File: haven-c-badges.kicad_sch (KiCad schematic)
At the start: 0 parts

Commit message: schematic done I think
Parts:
- added C1: 220nF, symbol Device:C
- added D1: LED, symbol Device:LED
- added L1: 25X48MM_NFC_ANTENNA, nfc_antenna:25X48MM_NFC_ANTENNA, symbol Device:L
- added R1: 47*, symbol Device:R
- added U1: NT3H2111W0FHKH, easyeda2kicad:XQFN-8_L1.6-W1.6-P0.50-BL_NT3H2111W0FHKH, symbol easyeda2kicad:NT3H2111W0FHKH
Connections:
- new net: C1.1, D1.1 (K), U1.2 (VSS)
- new net: D1.2 (A), R1.1
- new net: C1.2, R1.2, U1.6 (VCC), U1.7 (VOUT)
- new net: L1.2, U1.1 (LA)
- new net: L1.1, U1.8 (LB)
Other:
- note added: "NFC Stuff"
- note added: "This is from a guide I hope it isn't wrong"

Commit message: did some of that easyeda2kicad conversion and well.. yeah
- had some issues with courtyards and footprints not showing up
- set up env var paths I think
- i might just use part of notaroomba's library
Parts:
- C1: footprint (none) -> EasyEDA2Kicad:C0603
- D1: footprint (none) -> EasyEDA2Kicad:LED0805-R-RD
- L1: footprint nfc_antenna:25X48MM_NFC_ANTENNA -> EasyEDA2Kicad:25X48MM_NFC_ANTENNA manualimport
- R1: footprint (none) -> EasyEDA2Kicad:R0603
- U1: footprint easyeda2kicad:XQFN-8_L1.6-W1.6-P0.50-BL_NT3H2111W0FHKH -> EasyEDA2Kicad:XQFN-8_L1.6-W1.6-P0.50-BL_NT3H2111W0FHKH
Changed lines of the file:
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@@
 			)
 		)
-		(property "Footprint" ""
+		(property "Footprint" "EasyEDA2Kicad:LED0805-R-RD"
 			(at 107.95 123.19 0)
 			(hide yes)
@@
 			)
 		)
-		(property "Footprint" ""
+		(property "Footprint" "EasyEDA2Kicad:R0603"
 			(at 123.19 124.968 90)
 			(hide yes)
@@
 			)
 		)
-		(property "Footprint" ""
+		(property "Footprint" "EasyEDA2Kicad:C0603"
 			(at 119.38 108.2548 0)
 			(hide yes)
@@
 			)
 		)
-		(property "Footprint" "easyeda2kicad:XQFN-8_L1.6-W1.6-P0.50-BL_NT3H2111W0FHKH"
+		(property "Footprint" "EasyEDA2Kicad:XQFN-8_L1.6-W1.6-P0.50-BL_NT3H2111W0FHKH"
 			(at 115.57 100.33 0)
 			(hide yes)
@@
 			)
 		)
-		(property "Footprint" "nfc_antenna:25X48MM_NFC_ANTENNA"
+		(property "Footprint" "EasyEDA2Kicad:25X48MM_NFC_ANTENNA manualimport"
 			(at 115.57 66.04 0)
 			(hide yes)

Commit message: he was whipping up straight poison in a kettle
- WHY CANT I GET THESE TWO PADS TO CONNECT IDK ABOUT THE POLARITY pls help
- i switched all the footprints and symbols around like 3 times
- the antennas are wired up correctly now I think 💔(manual net assigning at the antenna pads)
a. polarity is not in antennas
b. but the nets not connected by default is rlly bugging me
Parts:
- removed U1: NT3H2111W0FHKH, EasyEDA2Kicad:XQFN-8_L1.6-W1.6-P0.50-BL_NT3H2111W0FHKH, symbol easyeda2kicad:NT3H2111W0FHKH
- added U1: NT3H2111W0FHKH, NFC Components:XQFN-8_L1.6-W1.6-P0.50-BL_NT3H2111W0FHKH, symbol NFC_components:NT3H2111W0FHKH
- L1: footprint EasyEDA2Kicad:25X48MM_NFC_ANTENNA manualimport -> NFC Components:25X48MM_NFC_ANTENNA
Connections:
- net at C1.1, D1.1 (K): now also U1.2 (VSS)
- net at C1.2, R1.2: now also U1.6 (VCC), U1.7 (VOUT)
- net at L1.2: now also U1.1 (LA)
- net at L1.1: now also U1.8 (LB)
- no-connect marks 0 -> 3
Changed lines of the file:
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@@
 		(color 0 0 0 0)
 	)
+	(no_connect
+		(at 105.41 90.17)
+	)
+	(no_connect
+		(at 105.41 92.71)
+	)
+	(no_connect
+		(at 125.73 92.71)
+	)
 	(wire
 		(pts
@@
 	(wire
 		(pts
-			(xy 129.54 66.04) (xy 119.38 66.04)
+			(xy 128.27 66.04) (xy 119.38 66.04)
 		)
 		(stroke
@@
 	(wire
 		(pts
-			(xy 101.6 85.09) (xy 105.41 85.09)
-		)
-		(stroke
-			(width 0)
-			(type default)
-		)
-	)
-	(wire
-		(pts
-			(xy 111.76 66.04) (xy 101.6 66.04)
-		)
-		(stroke
-			(width 0)
-			(type default)
-		)
-	)
-	(wire
-		(pts
-			(xy 125.73 85.09) (xy 129.54 85.09)
+			(xy 125.73 85.09) (xy 128.27 85.09)
+		)
+		(stroke
+			(width 0)
+			(type default)
+		)
+	)
+	(wire
+		(pts
+			(xy 111.76 66.04) (xy 102.87 66.04)
 		)
 		(stroke
@@
 	(wire
 		(pts
+			(xy 125.73 87.63) (xy 128.27 87.63)
+		)
+		(stroke
+			(width 0)
+			(type default)
+		)
+	)
+	(wire
+		(pts
 			(xy 100.33 87.63) (xy 100.33 123.19)
 		)
@@
 	(wire
 		(pts
-			(xy 129.54 85.09) (xy 129.54 66.04)
-		)
-		(stroke
-			(width 0)
-			(type default)
-		)
-	)
-	(wire
-		(pts
-			(xy 101.6 66.04) (xy 101.6 85.09)
-		)
-		(stroke
-			(width 0)
-			(type default)
-		)
-	)
-	(wire
-		(pts
-			(xy 127 87.63) (xy 125.73 87.63)
+			(xy 128.27 85.09) (xy 128.27 66.04)
+		)
+		(stroke
+			(width 0)
+			(type default)
+		)
+	)
+	(wire
+		(pts
+			(xy 102.87 66.04) (xy 102.87 85.09)
 		)
 		(stroke
@@
 	(wire
 		(pts
+			(xy 102.87 85.09) (xy 105.41 85.09)
+		)
+		(stroke
+			(width 0)
+			(type default)
+		)
+	)
+	(wire
+		(pts
 			(xy 100.33 87.63) (xy 102.87 87.63)
 		)
@@
 		(pts
 			(xy 111.76 123.19) (xy 119.38 123.19)
-		)
-		(stroke
-			(width 0)
-			(type default)
-		)
-	)
-	(wire
-		(pts
-			(xy 127 87.63) (xy 128.27 87.63)
 		)
 		(stroke
@@
 	)
 	(symbol
+		(lib_id "NFC_components:NT3H2111W0FHKH")
+		(at 115.57 88.9 0)
+		(unit 1)
+		(body_style 1)
+		(exclude_from_sim no)
+		(in_bom yes)
+		(on_board yes)
+		(in_pos_files yes)
+		(dnp no)
+		(fields_autoplaced yes)
+		(property "Reference" "U1"
+			(at 115.57 76.2 0)
+			(show_name no)
+			(do_not_autoplace no)
+			(effects
+				(font
+					(size 1.27 1.27)
+				)
+			)
+		)
+		(property "Value" "NT3H2111W0FHKH"
+			(at 115.57 78.74 0)
+			(show_name no)
+			(do_not_autoplace no)
+			(effects
+				(font
+					(size 1.27 1.27)
+				)
+			)
+		)
+		(property "Footprint" "NFC Components:XQFN-8_L1.6-W1.6-P0.50-BL_NT3H2111W0FHKH"
+			(at 115.57 100.33 0)
+			(hide yes)
+			(show_name no)
+			(do_not_autoplace no)
+			(effects
+				(font
+					(size 1.27 1.27)
+				)
+			)
+		)
+		(property "Datasheet" ""
+			(at 115.57 88.9 0)
+			(hide yes)
+			(show_name no)
+			(do_not_autoplace no)
+			(effects
+				(font
+					(size 1.27 1.27)
+				)
+			)
+		)
+		(property "Description" ""
+			(at 115.57 88.9 0)
+			(hide yes)
+			(show_name no)
+			(do_not_autoplace no)
+			(effects
+				(font
+					(size 1.27 1.27)
+				)
+			)
+		)
+		(property "LCSC Part" "C710403"
+			(at 115.57 102.87 0)
+			(hide yes)
+			(show_name no)
+			(do_not_autoplace no)
+			(effects
+				(font
+					(size 1.27 1.27)
+				)
+			)
+		)
+		(pin "2"
+		)
+		(pin "6"
+		)
+		(pin "3"
+		)
+		(pin "5"
+		)
+		(pin "8"
+		)
+		(pin "7"
+		)
+		(pin "1"
+		)
+		(pin "4"
+		)
+		(instances
+			(project "haven-c-badges"
+				(path "/a388d1d2-d6b4-4bc6-8c80-be157f48129c"
+					(reference "U1")
+					(unit 1)
+				)
+			)
+		)
+	)
+	(symbol
 		(lib_id "Device:C")
 		(at 115.57 109.22 90)
@@
 				(path "/a388d1d2-d6b4-4bc6-8c80-be157f48129c"
 					(reference "C1")
-					(unit 1)
-				)
-			)
-		)
-	)
-	(symbol
-		(lib_id "easyeda2kicad:NT3H2111W0FHKH")
-		(at 115.57 88.9 0)
-		(unit 1)
-		(body_style 1)
-		(exclude_from_sim no)
-		(in_bom yes)
-		(on_board yes)
-		(in_pos_files yes)
-		(dnp no)
-		(fields_autoplaced yes)
-		(property "Reference" "U1"
-			(at 115.57 77.47 0)
-			(show_name no)
-			(do_not_autoplace no)
-			(effects
-				(font
-					(size 1.27 1.27)
-				)
-			)
-		)
-		(property "Value" "NT3H2111W0FHKH"
-			(at 115.57 80.01 0)
-			(show_name no)
-			(do_not_autoplace no)
-			(effects
-				(font
-					(size 1.27 1.27)
-				)
-			)
-		)
-		(property "Footprint" "EasyEDA2Kicad:XQFN-8_L1.6-W1.6-P0.50-BL_NT3H2111W0FHKH"
-			(at 115.57 100.33 0)
-			(hide yes)
-			(show_name no)
-			(do_not_autoplace no)
-			(effects
-				(font
-					(size 1.27 1.27)
-				)
-			)
-		)
-		(property "Datasheet" "https://www.lcsc.com/datasheet/C710403.pdf"
-			(at 115.57 102.87 0)
-			(hide yes)
-			(show_name no)
-			(do_not_autoplace no)
-			(effects
-				(font
-					(size 1.27 1.27)
-				)
-			)
-		)
-		(property "Description" ""
-			(at 115.57 88.9 0)
-			(hide yes)
-			(show_name no)
-			(do_not_autoplace no)
-			(effects
-				(font
-					(size 1.27 1.27)
-				)
-			)
-		)
-		(property "Manufacturer" "NXP(恩智浦)"
-			(at 115.57 105.41 0)
-			(hide yes)
-			(show_name no)
-			(do_not_autoplace no)
-			(effects
-				(font
-					(size 1.27 1.27)
-				)
-			)
-		)
-		(property "MPN" "NT3H2111W0FHKH"
-			(at 115.57 107.95 0)
-			(hide yes)
-			(show_name no)
-			(do_not_autoplace no)
-			(effects
-				(font
-					(size 1.27 1.27)
-				)
-			)
-		)
-		(property "LCSC Part" "C710403"
-			(at 115.57 110.49 0)
-			(hide yes)
-			(show_name no)
-			(do_not_autoplace no)
-			(effects
-				(font
-					(size 1.27 1.27)
-				)
-			)
-		)
-		(pin "1"
-		)
-		(pin "8"
-		)
-		(pin "3"
-		)
-		(pin "6"
-		)
-		(pin "7"
-		)
-		(pin "5"
-		)
-		(pin "2"
-		)
-		(pin "4"
-		)
-		(instances
-			(project "haven-c-badges"
-				(path "/a388d1d2-d6b4-4bc6-8c80-be157f48129c"
-					(reference "U1")
 					(unit 1)
 				)
@@
 			)
 		)
-		(property "Footprint" "EasyEDA2Kicad:25X48MM_NFC_ANTENNA manualimport"
+		(property "Footprint" "NFC Components:25X48MM_NFC_ANTENNA"
 			(at 115.57 66.04 0)
 			(hide yes)

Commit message: idk some scaling adjustment things
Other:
- moved on the sheet: C1, D1, L1, R1, U1

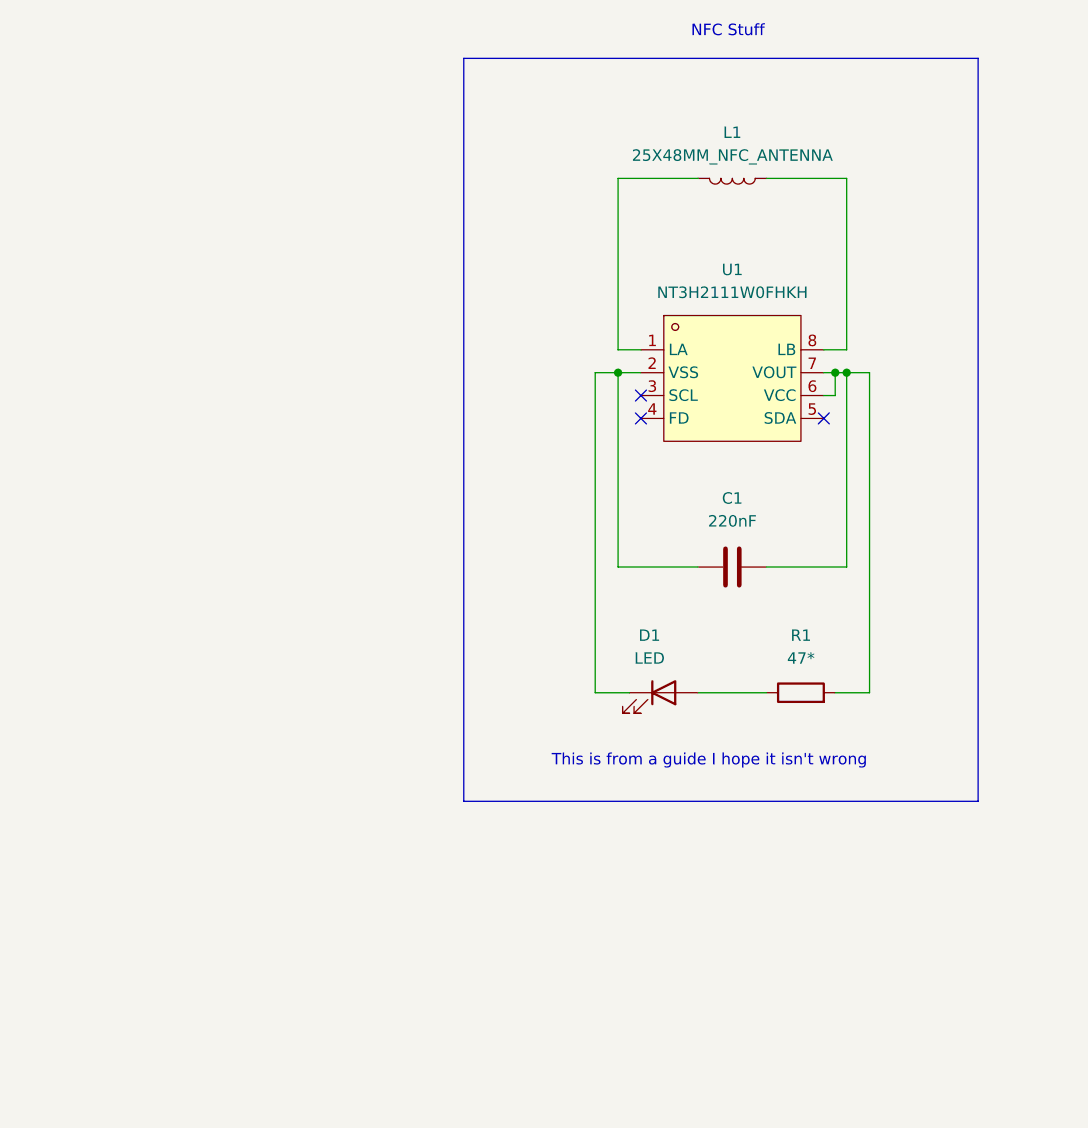
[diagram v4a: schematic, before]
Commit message: edited schematics with name & resize + edited the solder mask mask
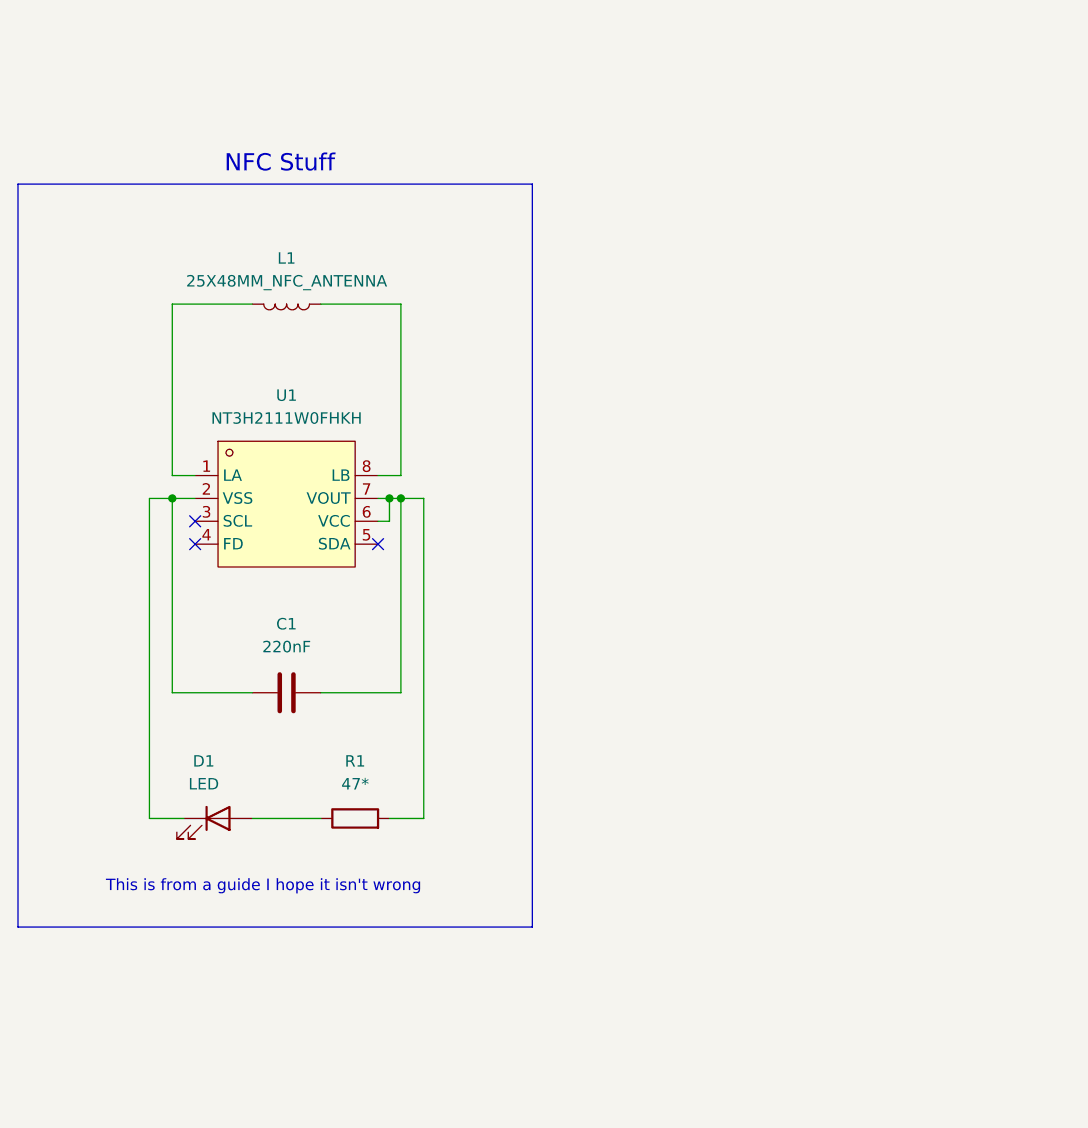
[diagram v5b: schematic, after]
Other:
- title: (none) -> Haven C Badges
- moved on the sheet: C1, D1, L1, R1, U1
